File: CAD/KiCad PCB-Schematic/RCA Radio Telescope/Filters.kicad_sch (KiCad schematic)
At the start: 9 parts, among them U3 SKY13588-460LF, U4 SKY13588-460LF, U5 SN74AVC2T244DQER, U6 MIC5365-1.8YC5-TR, U7 MIC5365-3.3YC5-TR

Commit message: Updated PowerDataDistribute Schematic to v1.3
- Added 5V to 3V Buck for LNA
- Added TVS diode, PMOS, and polyfuse for power protection (need to select PMOS and polyfuse)
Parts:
- U3, U4: footprint Library:QFN12_SKY -> QFN12_SKY
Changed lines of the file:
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@@
 	(label "INT_CTRL_V2"
 		(at 86.36 111.76 0)
+		(fields_autoplaced yes)
 		(effects
 			(font
@@
 	(label "INT_CTRL_V1"
 		(at 86.36 109.22 0)
+		(fields_autoplaced yes)
 		(effects
 			(font
@@
 	(label "FILTERB_OUT"
 		(at 266.7 72.39 0)
+		(fields_autoplaced yes)
 		(effects
 			(font
@@
 	(label "FILTERB_OUT"
 		(at 54.61 59.69 180)
+		(fields_autoplaced yes)
 		(effects
 			(font
@@
 	(label "FILTERA_IN"
 		(at 142.24 25.4 180)
+		(fields_autoplaced yes)
 		(effects
 			(font
@@
 	(label "FILTERA_IN"
 		(at 91.44 26.67 0)
+		(fields_autoplaced yes)
 		(effects
 			(font
@@
 	(label "INT_CTRL_V1"
 		(at 92.71 81.28 0)
+		(fields_autoplaced yes)
 		(effects
 			(font
@@
 	(label "INT_CTRL_V2"
 		(at 50.8 48.26 180)
+		(fields_autoplaced yes)
 		(effects
 			(font
@@
 	(label "INT_CTRL_V1"
 		(at 50.8 45.72 180)
+		(fields_autoplaced yes)
 		(effects
 			(font
@@
 	(label "FILTERC_OUT"
 		(at 266.7 125.73 0)
+		(fields_autoplaced yes)
 		(effects
 			(font
@@
 	(label "FILTERB_IN"
 		(at 142.24 73.66 180)
+		(fields_autoplaced yes)
 		(effects
 			(font
@@
 	(label "FILTERA_OUT"
 		(at 54.61 62.23 180)
+		(fields_autoplaced yes)
 		(effects
 			(font
@@
 	(label "FILTERC_IN"
 		(at 142.24 124.46 180)
+		(fields_autoplaced yes)
 		(effects
 			(font
@@
 	(label "FILTERA_OUT"
 		(at 265.43 26.67 0)
+		(fields_autoplaced yes)
 		(effects
 			(font
@@
 	(label "INT_CTRL_V2"
 		(at 92.71 78.74 0)
+		(fields_autoplaced yes)
 		(effects
 			(font
@@
 	(label "FILTERC_IN"
 		(at 91.44 31.75 0)
+		(fields_autoplaced yes)
 		(effects
 			(font
@@
 	(label "FILTERB_IN"
 		(at 91.44 29.21 0)
+		(fields_autoplaced yes)
 		(effects
 			(font
@@
 	(label "FILTERC_OUT"
 		(at 54.61 64.77 180)
+		(fields_autoplaced yes)
 		(effects
 			(font
@@
 		(shape input)
 		(at 62.23 118.11 180)
+		(fields_autoplaced yes)
 		(effects
 			(font
@@
 		(shape input)
 		(at 62.23 115.57 180)
+		(fields_autoplaced yes)
 		(effects
 			(font
@@
 		(shape bidirectional)
 		(at 109.22 59.69 0)
+		(fields_autoplaced yes)
 		(effects
 			(font
@@
 		(shape input)
 		(at 43.18 135.89 180)
+		(fields_autoplaced yes)
 		(effects
 			(font
@@
 		(shape bidirectional)
 		(at 33.02 26.67 180)
+		(fields_autoplaced yes)
 		(effects
 			(font
@@
 		(shape input)
 		(at 38.1 107.95 180)
+		(fields_autoplaced yes)
 		(effects
 			(font
@@
 			)
 		)
-		(property "Footprint" "Library:QFN12_SKY"
+		(property "Footprint" "QFN12_SKY"
 			(at 76.2 53.086 0)
 			(effects
@@
 			)
 		)
-		(property "Footprint" "Library:QFN12_SKY"
+		(property "Footprint" "QFN12_SKY"
 			(at 72.644 84.074 0)
 			(effects

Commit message: Updated PowerDataDistribute schematicto v1.4
- Added components for fuses and PMOS
- Created PCB v1.0
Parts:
- U3, U4: footprint QFN12_SKY -> Library:QFN12_SKY
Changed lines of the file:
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@@
 			)
 		)
-		(property "Footprint" "QFN12_SKY"
+		(property "Footprint" "Library:QFN12_SKY"
 			(at 76.2 53.086 0)
 			(effects
@@
 			)
 		)
-		(property "Footprint" "QFN12_SKY"
+		(property "Footprint" "Library:QFN12_SKY"
 			(at 72.644 84.074 0)
 			(effects

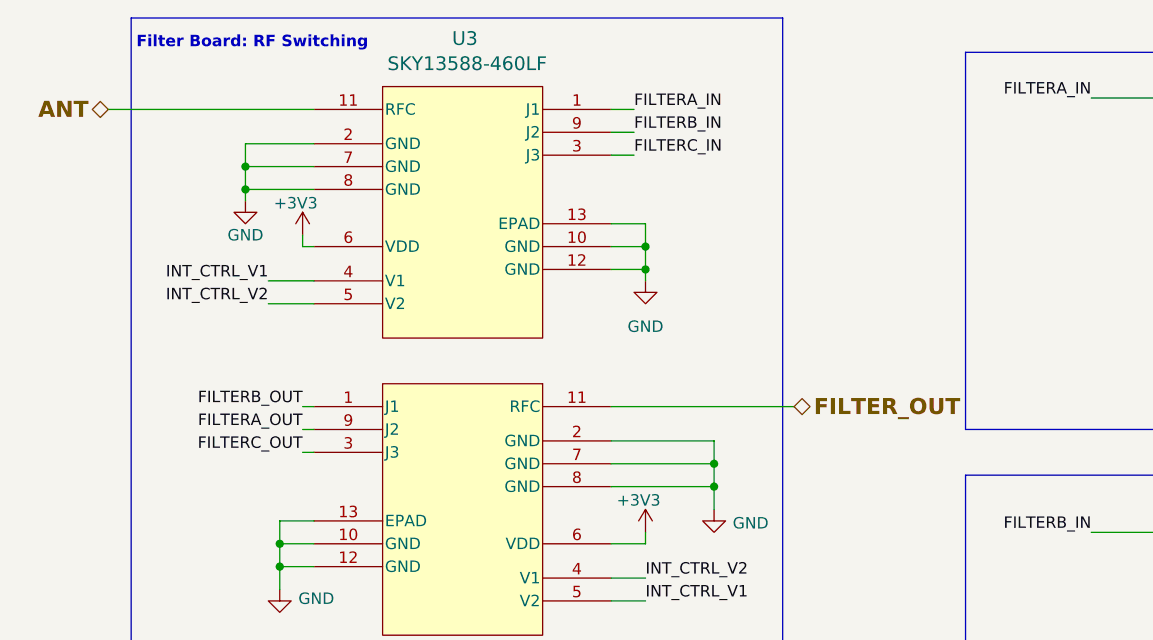
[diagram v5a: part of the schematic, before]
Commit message: BOM Update and Schematic Update
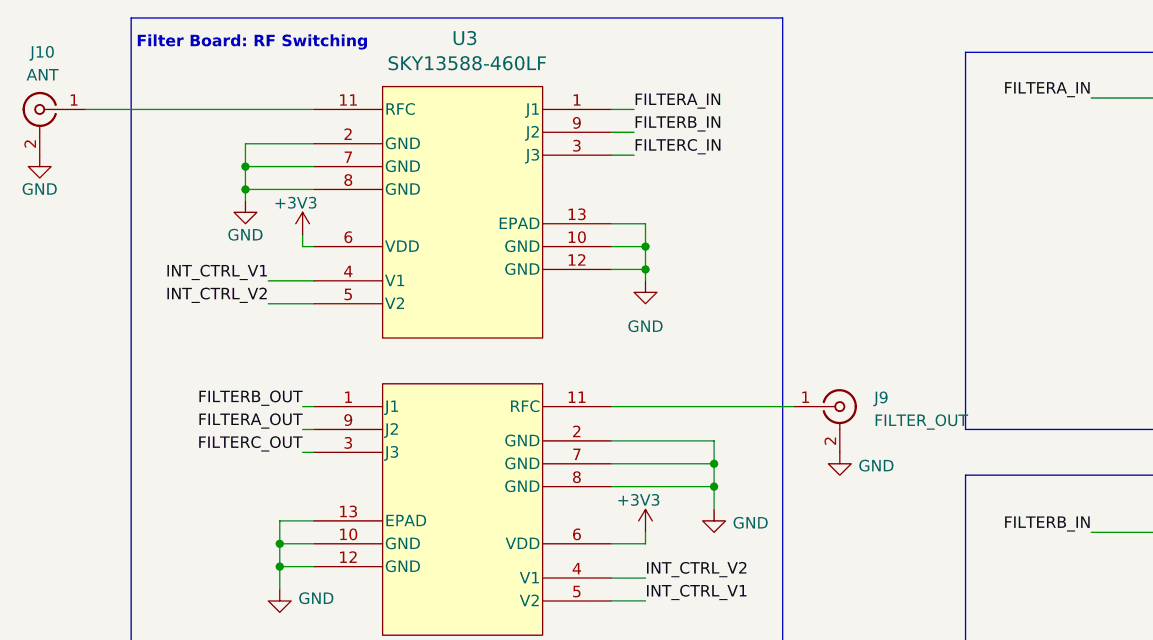
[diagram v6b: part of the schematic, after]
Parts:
- added J10: ANT, symbol Connector:Conn_Coaxial
- added J9: FILTER_OUT, symbol Connector:Conn_Coaxial
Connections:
- net GND: now also J10.2 (Ext), J9.2 (Ext)
- net ANT: no longer names the net of U3.11 (RFC)
- net ANT: now also J10.1 (In)
- net FILTER_OUT: no longer names the net of U4.11 (RFC)
- net FILTER_OUT: now also J9.1 (In)

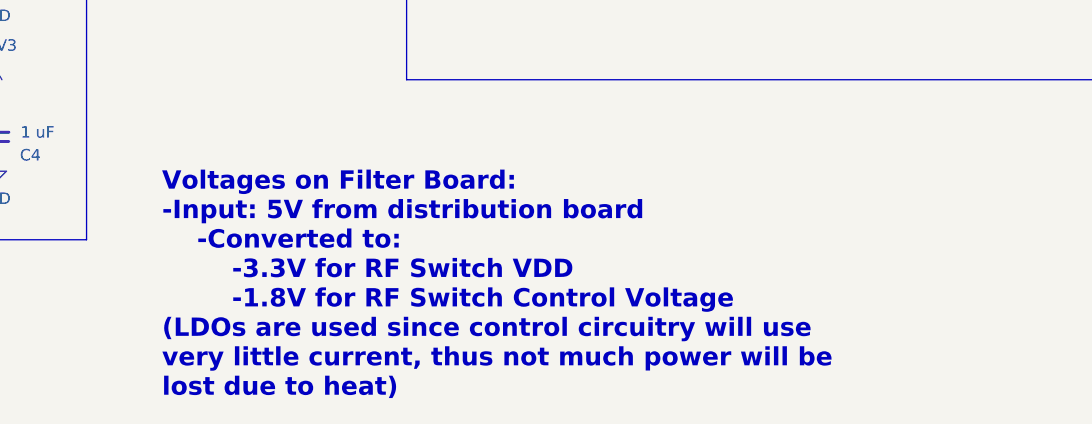
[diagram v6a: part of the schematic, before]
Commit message: Updated PowerData Board to v1.2
- Added zone fills for certain pins
- Added ground vias for mounting holes
- Minor readjustments to components
- Added silkscreen for voltage polarity
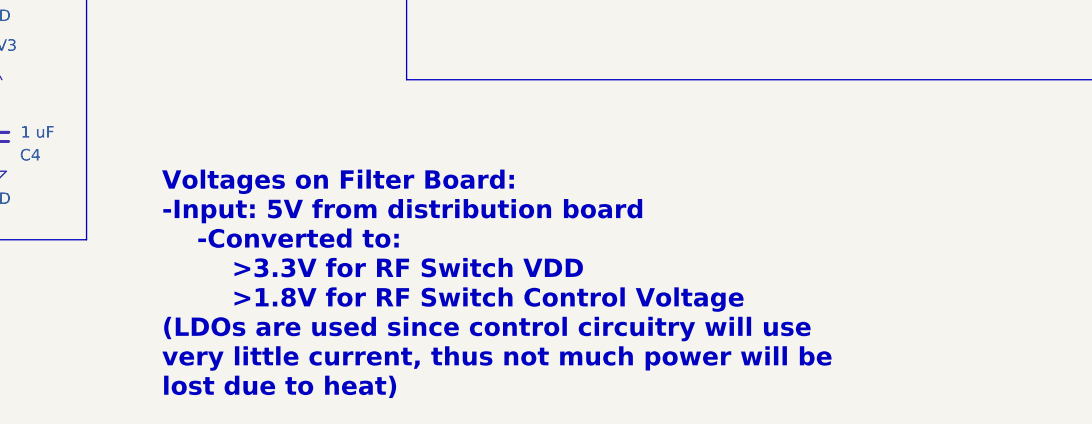
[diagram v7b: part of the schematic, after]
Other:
- note added: "Voltages on Filter Board: -Input: 5V from distribution board -Converted to: >3.3V for RF Switch VDD >1.8V for RF Switch Control Voltage (LDOs are used since control circuitry will use very little current, thus not much power will be lost due to heat)"
- note removed: "Voltages on Filter Board: -Input: 5V from distribution board -Converted to: -3.3V for RF Switch VDD -1.8V for RF Switch Control Voltage (LDOs are used since control circuitry will use very little current, thus not much power will be lost due to heat)"
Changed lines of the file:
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@@
 		)
 	)
-	(text "Voltages on Filter Board:\n-Input: 5V from distribution board\n	-Converted to:\n		-3.3V for RF Switch VDD\n		-1.8V for RF Switch Control Voltage\n(LDOs are used since control circuitry will use \nvery little current, thus not much power will be \nlost due to heat)"
+	(text "Voltages on Filter Board:\n-Input: 5V from distribution board\n	-Converted to:\n		>3.3V for RF Switch VDD\n		>1.8V for RF Switch Control Voltage\n(LDOs are used since control circuitry will use \nvery little current, thus not much power will be \nlost due to heat)"
 		(exclude_from_sim no)
 		(at 101.092 180.34 0)
